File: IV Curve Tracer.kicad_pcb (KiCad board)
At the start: 2 copper layers, 130 x 80 mm, 75 parts, among them IC1 MAX680ESA+, J0 TB002-500-02BE, J1 CAN_Out, J5 Conn_01x15, J6 Conn_01x15, J7 CAN_In, Q1 IRF100P218XKMA1, Q2 IRF100P218XKMA1, SW0 SW_Rotary2x3, U1 INA211CQDCKRQ1, U2 LT1215, U3 LT1215, U4 ADM3055E, U5 CDSOT23-T24CAN

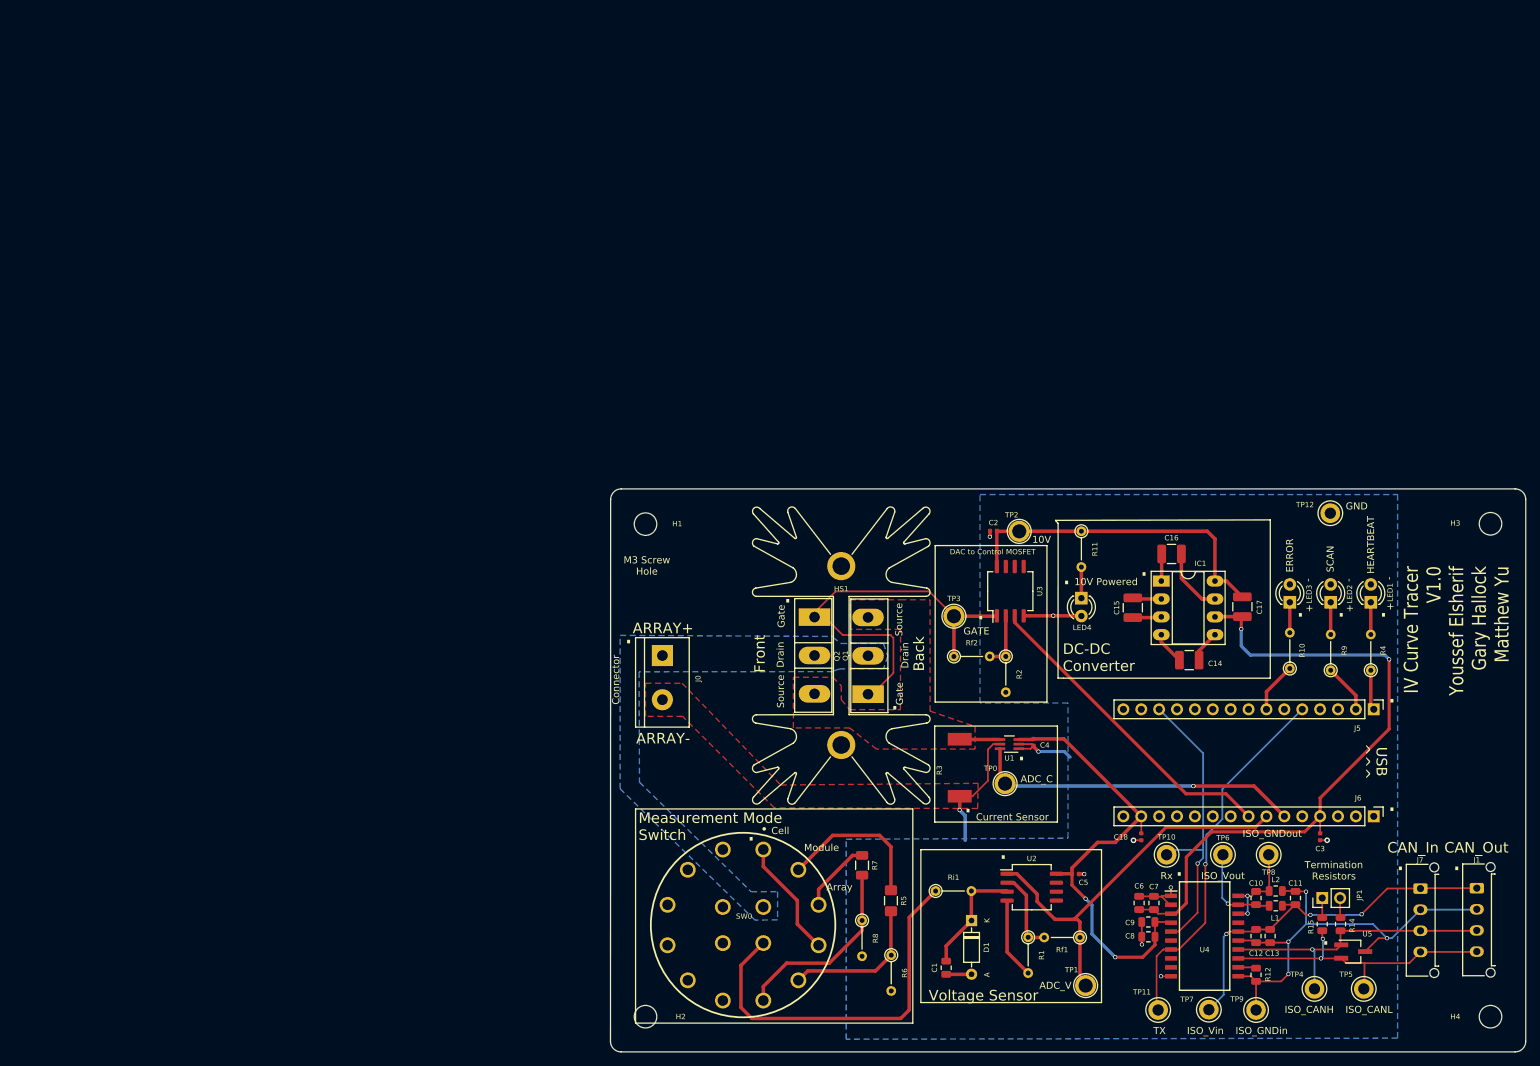
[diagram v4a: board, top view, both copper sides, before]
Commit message: Major Curve Tracer Board overhaul. Schematic advanced to Rev 1.1.0. Layout advanced to Rev 1.1.0. Parts list advanced to Rev 1.1.0.
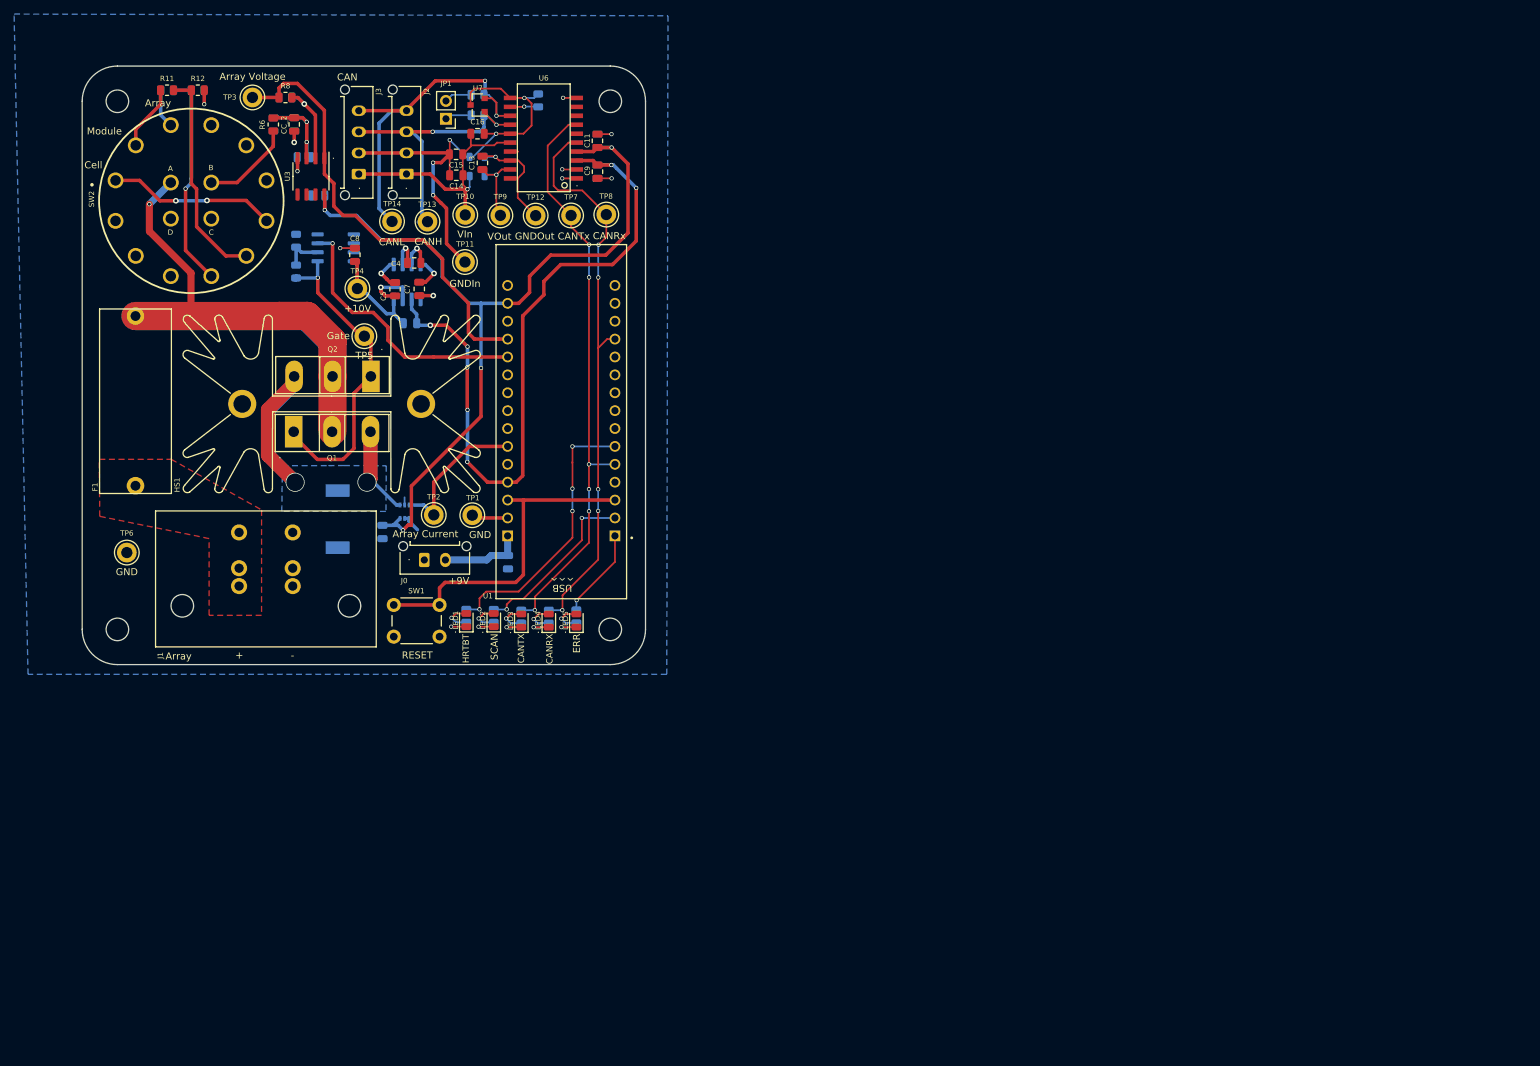
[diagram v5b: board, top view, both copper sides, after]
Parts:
- removed C17: 4.7uF, Capacitor_SMD:C_1210_3225Metric
- removed C18, C2: .1uF, Capacitor_SMD:C_0402_1005Metric
- removed IC1: MAX680ESA+, Package_DIP:DIP-8_W7.62mm_Socket_LongPads
- removed J5, J6: Conn_01x15, Connector_PinHeader_2.54mm:PinHeader_1x15_P2.54mm_Vertical
- removed J7: CAN_In, Connector_Molex:Molex_Micro-Fit_3.0_43650-0415_1x04_P3.00mm_Vertical
- removed Rf1: 1k, Resistor_THT:R_Axial_DIN0204_L3.6mm_D1.6mm_P5.08mm_Vertical
- removed Rf2: 4k, Resistor_THT:R_Axial_DIN0204_L3.6mm_D1.6mm_P5.08mm_Vertical
- removed Ri1: 10k, Resistor_THT:R_Axial_DIN0204_L3.6mm_D1.6mm_P5.08mm_Vertical
- removed SW0: SW_Rotary2x3, CK1052:CK1052
- removed TP0: TestPoint, TestPoint:TestPoint_Plated_Hole_D2.0mm
- added C0: .1uF, Capacitor_SMD:C_0805_2012Metric, B.Cu at (80.5, 90.5)
- added CA_2: .01uF, Capacitor_SMD:C_0805_2012Metric, B.Cu at (51.5, 32.9)
- added CB_2: .01uF, Capacitor_SMD:C_0805_2012Metric, B.Cu at (50.1, 28.3)
- added CC_2: .01uF, Capacitor_SMD:C_0805_2012Metric, F.Cu at (50.1, 28.3)
- added F1: Fuse, IV Curve Tracer:05200101Z_Fuze_Holder_5x20_PCB_Mount, F.Cu at (32.7, 54.5)
- added G***: LOGO, UTSVT_Special:UTSVT_Logo_Symbol, B.Cu at (88.2, 47.2)
- added G***: LOGO, UTSVT_Special:Hallock_Image_Small, B.Cu at (88.2, 75.6)
- added J2: CAN_In, Connector_Molex:Molex_Micro-Fit_3.0_43650-0415_1x04_P3.00mm_Vertical, F.Cu at (66.1, 35.3)
- added J3: CAN_Out, Connector_Molex:Molex_Micro-Fit_3.0_43650-0415_1x04_P3.00mm_Vertical, F.Cu at (59.3, 35.3)
- added LED5: Error (Amber), LED_SMD:LED_0805_2012Metric, F.Cu at (90.2, 98.8)
- added R13: 132k, Resistor_SMD:R_0805_2012Metric, B.Cu at (32.1, 23.4)
- added R16: 0, Resistor_SMD:R_0805_2012Metric, B.Cu at (84.8, 24.9)
- added R17: 60, Resistor_SMD:R_0805_2012Metric, B.Cu at (76.2, 27.0)
- added R18: 60, Resistor_SMD:R_0805_2012Metric, B.Cu at (76.2, 24.1)
- added SW1: SW_Push, Button_Switch_THT:SW_PUSH_6mm, F.Cu at (70.8, 101.0)
- added SW2: A20303RNCG, IV Curve Tracer:A20303RNCG_rotary_sw_dp3t, F.Cu at (35.5, 39.1)
- added TP13: CAN_H, TestPoint:TestPoint_Keystone_5005-5009_Compact, F.Cu at (69.0, 42.1)
- added TP14: CAN_L, TestPoint:TestPoint_Keystone_5005-5009_Compact, F.Cu at (64.0, 42.1)
- added U6: ADM3055E, IV Curve Tracer:ADM3055EBRIZ, F.Cu at (85.5, 30.2)
- added U7: CDSOT23-T24CAN, Package_TO_SOT_SMD:SOT-23, F.Cu at (76.2, 25.5)
- C1: value Variable -> .1uF; moved to B.Cu
- C10: value 0.22uF -> .1uF; moved to B.Cu
- C11: value 10uF -> .1uF
- C12: value 0.1uF -> .01uF; moved to B.Cu
- C13: value 0.01uF -> .22uF
- C14: value 4.7uF -> 10uF; footprint Capacitor_SMD:C_1210_3225Metric -> Capacitor_SMD:C_0805_2012Metric
- C15: value 4.7uF -> .1uF; footprint Capacitor_SMD:C_1210_3225Metric -> Capacitor_SMD:C_0805_2012Metric
- C16: value 4.7uF -> .01uF; footprint Capacitor_SMD:C_1210_3225Metric -> Capacitor_SMD:C_0805_2012Metric
- C3: footprint Capacitor_SMD:C_0402_1005Metric -> Capacitor_SMD:C_0805_2012Metric; moved to B.Cu
- C4, C5: value .1uF -> 4.7uF; footprint Capacitor_SMD:C_0402_1005Metric -> Capacitor_SMD:C_0805_2012Metric
- C6: value 10uF -> 4.7uF; moved to B.Cu
- C7: value 0.1uF -> 4.7uF
- C8: value 0.1uF -> .1uF
- C9: value 0.01uF -> 10uF
- D1: value 1N5226B-B -> 3.9V Zener; footprint Diode_THT:D_DO-35_SOD27_P7.62mm_Horizontal -> Diode_SMD:D_0805_2012Metric; moved to B.Cu
- J0: value TB002-500-02BE -> 9V Supply; footprint IV Curve Tracer:ExpandedBlockTerminal-2H_P7.62mm -> Connector_Molex:Molex_Micro-Fit_3.0_43650-0215_1x02_P3.00mm_Vertical
- J1: value CAN_Out -> Solar Array; footprint Connector_Molex:Molex_Micro-Fit_3.0_43650-0415_1x04_P3.00mm_Vertical -> IV Curve Tracer:PhoenixContact_PowerCombicon5_GF_2x7.62mm
- L1, L2: value 2kH -> 1.8kH; moved to B.Cu
- LED1: value TLHR5400-AS12Z -> Heartbeat (Blue); footprint LED_THT:LED_D3.0mm -> LED_SMD:LED_0805_2012Metric
- LED2: value TLHR5400-AS12Z -> Scanning (Blue); footprint LED_THT:LED_D3.0mm -> LED_SMD:LED_0805_2012Metric
- LED3: value TLHR5400-AS12Z -> CAN_Rx (Blue); footprint LED_THT:LED_D3.0mm -> LED_SMD:LED_0805_2012Metric
- LED4: value TLHR5400-AS12Z -> CAN_Tx (Blue); footprint LED_THT:LED_D3.0mm -> LED_SMD:LED_0805_2012Metric
- R1, R2: value 1k -> 330; footprint Resistor_THT:R_Axial_DIN0204_L3.6mm_D1.6mm_P5.08mm_Vertical -> Resistor_SMD:R_0805_2012Metric; moved to B.Cu
- R10: value 330 -> 1k; footprint Resistor_THT:R_Axial_DIN0204_L3.6mm_D1.6mm_P5.08mm_Vertical -> Resistor_SMD:R_0805_2012Metric; moved to B.Cu
- R11: value 1k -> 56.6k; footprint Resistor_THT:R_Axial_DIN0204_L3.6mm_D1.6mm_P5.08mm_Vertical -> Resistor_SMD:R_0805_2012Metric
- R12: value 0 -> 10k
- R14: value 60 -> 2k; moved to B.Cu
- R15: value 60 -> .5m; footprint Resistor_SMD:R_0805_2012Metric -> IV Curve Tracer:R-WSLF2512L5000FEB; moved to B.Cu
- R3: value R3: WSLF2512L5000FEB (.5mO) -> 330; footprint IV Curve Tracer:R-WSLF2512L5000FEB -> Resistor_SMD:R_0805_2012Metric; moved to B.Cu
- R4: footprint Resistor_THT:R_Axial_DIN0204_L3.6mm_D1.6mm_P5.08mm_Vertical -> Resistor_SMD:R_0805_2012Metric; moved to B.Cu
- R5: value R5: RN732BTTD56R6F50 (56.6k) -> 330; footprint Resistor_SMD:R_1206_3216Metric_Pad1.42x1.75mm_HandSolder -> Resistor_SMD:R_0805_2012Metric; moved to B.Cu
- R6: footprint Resistor_THT:R_Axial_DIN0204_L3.6mm_D1.6mm_P5.08mm_Vertical -> Resistor_SMD:R_0805_2012Metric
- R7: value R7: RN73H2BTTD1323F25 (132kO) -> 1k; footprint Resistor_SMD:R_1206_3216Metric -> Resistor_SMD:R_0805_2012Metric; moved to B.Cu
- R8: value 2k -> 1k; footprint Resistor_THT:R_Axial_DIN0204_L3.6mm_D1.6mm_P5.08mm_Vertical -> Resistor_SMD:R_0805_2012Metric
- R9: value 330 -> 4k; footprint Resistor_THT:R_Axial_DIN0204_L3.6mm_D1.6mm_P5.08mm_Vertical -> Resistor_SMD:R_0805_2012Metric; moved to B.Cu
- TP1: value TestPoint -> GND; footprint TestPoint:TestPoint_Plated_Hole_D2.0mm -> TestPoint:TestPoint_Keystone_5005-5009_Compact
- TP10: value CAN_Rx -> CAN_ISO_Vin
- TP11: value CAN_Tx -> CAN_ISO_GndIn
- TP12: value GroundTP -> CAN_ISO_GndOut
- TP2: value TestPoint -> Array Current; footprint TestPoint:TestPoint_Plated_Hole_D2.0mm -> TestPoint:TestPoint_Keystone_5005-5009_Compact
- TP3: value TestPoint -> Array Voltage; footprint TestPoint:TestPoint_Plated_Hole_D2.0mm -> TestPoint:TestPoint_Keystone_5005-5009_Compact
- TP4: value CAN_H -> +10V
- TP5: value CAN_L -> Gate
- TP6: value ISO_Vout -> GND
- TP7: value ISO_Vin -> CAN_Tx
- TP8: value ISO_GNDout -> CAN_Rx
- TP9: value ISO_GNDin -> CAN_ISO_Vout
- U1: value INA211CQDCKRQ1 -> MCU_Nucleo_L432KC; footprint Package_TO_SOT_SMD:SOT-363_SC-70-6_Handsoldering -> IV Curve Tracer:MODULE_NUCLEO-L432KC
- U2: value LT1215 -> INA211; footprint Package_SO:SO-8_5.3x6.2mm_P1.27mm -> IV Curve Tracer:SC70-6; moved to B.Cu
- U3: footprint Package_SO:SO-8_5.3x6.2mm_P1.27mm -> Package_SO:SO-8_3.9x4.9mm_P1.27mm
- U4: value ADM3055E -> MAX680ESA+; footprint SamacSys_Parts:SOIC127P1030X264-20N -> Package_SO:SOIC-8_3.9x4.9mm_P1.27mm; moved to B.Cu
- U5: value CDSOT23-T24CAN -> LT1215; footprint Package_TO_SOT_SMD:SOT-23W_Handsoldering -> Package_SO:SO-8_3.9x4.9mm_P1.27mm; moved to B.Cu
- moved R14 200.9 mm to (36.4, 23.4), turned to 0 degrees
- moved R12 195.9 mm to (36.4, 23.4), turned to 0 degrees
- moved H3 195.6 mm to (25.0, 100.0)
- moved J1 182.9 mm to (42.3, 86.2), turned to 0 degrees
- moved U5 175.7 mm to (56.0, 45.8)
- moved TP5 169.5 mm to (60.1, 58.4), turned to 180 degrees
- moved C3 168.9 mm to (53.5, 38.4), turned to 0 degrees
- moved TP4 168.4 mm to (59.1, 51.6), turned to 180 degrees
- moved JP1 166.5 mm to (71.7, 27.5), turned to 180 degrees
- moved TP6 161.5 mm to (26.3, 89.1)
- moved R9 157.5 mm to (50.4, 49.2)
- moved C13 156.7 mm to (76.8, 33.8), turned to 90 degrees
- moved TP9 155.7 mm to (79.4, 41.2)
- moved L2 154.1 mm to (76.1, 32.9), turned to 0 degrees
- moved R10 153.6 mm to (50.4, 44.8)
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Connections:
- C1 pad 1: GND -> +3V3
- C1 pad 2: Net-(C1-Pad2) -> GND
- C10 pad 1: Net-(C10-Pad1) -> +5V
- C10 pad 2: Net-(C10-Pad2) -> GND
- C11 pad 1: Net-(C11-Pad1) -> +3V3
- C11 pad 2: Net-(C11-Pad2) -> GND
- C12 pad 1: Net-(C11-Pad1) -> +3V3
- C12 pad 2: Net-(C11-Pad2) -> GND
- C13 pad 1: Net-(C11-Pad1) -> Net-(C13-Pad1)
- C13 pad 2: Net-(C11-Pad2) -> Net-(C13-Pad2)
- C14 pad 1: -10V -> Net-(C14-Pad1)
- C14 pad 2: GND -> Net-(C14-Pad2)
- C15 pad 1: Net-(C15-Pad1) -> Net-(C14-Pad1)
- C15 pad 2: Net-(C15-Pad2) -> Net-(C14-Pad2)
- C16 pad 1: Net-(C16-Pad1) -> Net-(C14-Pad1)
- C16 pad 2: Net-(C16-Pad2) -> Net-(C14-Pad2)
- C3 pad 1: +5V -> GND
- C3 pad 2: GND -> +3V3
- C4 pad 1: GND -> Net-(C4-Pad1)
- C4 pad 2: +3V3 -> Net-(C4-Pad2)
- C5 pad 1: GND -> Net-(C5-Pad1)
- C5 pad 2: +3V3 -> Net-(C5-Pad2)
- C6 pad 1: +5V -> +10V
- C6 pad 2: GND -> +5V
- C7 pad 1: +5V -> GND
- C7 pad 2: GND -> -10V
- C8 pad 1: +3V3 -> GND
- C8 pad 2: GND -> +10V
- C9 pad 1: +3V3 -> +5V
- D1 pad 1: Net-(C1-Pad2) -> Net-(CA_2-Pad1)
- J0 pad 1: Net-(J0-Pad1) -> GND
- J0 pad 2: GND -> +9V
- J1 pad 1: Net-(C11-Pad1) -> Net-(F1-Pad2)
- J1 pad 2: Net-(C11-Pad2) -> GND
- JP1 pad 1: /TERM_L -> Net-(JP1-Pad1)
- JP1 pad 2: /TERM_H -> Net-(JP1-Pad2)
- L1 pad 1: Net-(C11-Pad1) -> Net-(C14-Pad1)
- L1 pad 2: Net-(C10-Pad1) -> Net-(C13-Pad1)
- L2 pad 1: Net-(C11-Pad2) -> Net-(C14-Pad2)
- L2 pad 2: Net-(C10-Pad2) -> Net-(C13-Pad2)
- LED1 pad 1: Net-(LED1-Pad1) -> GND
- LED1 pad 2: GND -> Net-(LED1-Pad2)
- LED2 pad 1: Net-(LED2-Pad1) -> GND
- LED2 pad 2: GND -> Net-(LED2-Pad2)
- LED3 pad 1: Net-(LED3-Pad1) -> GND
- LED3 pad 2: GND -> Net-(LED3-Pad2)
- LED4 pad 1: Net-(LED4-Pad1) -> GND
- LED4 pad 2: GND -> Net-(LED4-Pad2)
- Q1 pad 1: GATE -> /Gate
- Q1 pad 2: Net-(J0-Pad1) -> Net-(F1-Pad1)
- Q1 pad 3: Net-(Q1-Pad3) -> /+Current_Sense
- Q2 pad 1: GATE -> /Gate
- Q2 pad 2: Net-(J0-Pad1) -> Net-(F1-Pad1)
- Q2 pad 3: Net-(Q1-Pad3) -> /+Current_Sense
- R1 pad 1: Net-(R1-Pad1) -> Net-(LED1-Pad2)
- R1 pad 2: GND -> /Heartbeat
- R10 pad 1: Net-(J5-Pad7) -> Net-(R10-Pad1)
- R10 pad 2: Net-(LED3-Pad1) -> GND
- R11 pad 1: +10V -> Net-(R11-Pad1)
- R11 pad 2: Net-(LED4-Pad1) -> Net-(R11-Pad2)
- R12 pad 1: /RSlope -> Net-(R11-Pad2)
- R12 pad 2: Net-(C11-Pad2) -> GND
- R14 pad 1: /TERM_H -> Net-(R13-Pad2)
- R14 pad 2: /CAN_H -> GND
- R15 pad 1: /TERM_L -> GND
- R15 pad 2: /CAN_L -> /+Current_Sense
- R2 pad 1: Net-(R2-Pad1) -> Net-(LED2-Pad2)
- R2 pad 2: GND -> /Scanning
- R3 pad 1: GND -> Net-(LED3-Pad2)
- R3 pad 2: Net-(Q1-Pad3) -> /CAN_Rx
- R4 pad 1: Net-(J5-Pad1) -> Net-(LED4-Pad2)
- R4 pad 2: Net-(LED1-Pad1) -> /CAN_Tx
- R5 pad 2: Net-(R5-Pad2) -> /Error
- R6 pad 1: Net-(R5-Pad2) -> /Voltage_Sense
- R6 pad 2: GND -> Net-(CA_2-Pad1)
- R7 pad 2: Net-(R7-Pad2) -> GND
- R8 pad 1: Net-(R7-Pad2) -> /Array_Voltage
- R8 pad 2: GND -> Net-(R7-Pad1)
- R9 pad 1: Net-(J5-Pad2) -> /Gate
- R9 pad 2: Net-(LED2-Pad1) -> Net-(R10-Pad1)
- TP1 pad 1: ADC_V -> GND
- TP10 pad 1: CAN_RX -> Net-(C14-Pad1)
- TP11 pad 1: CAN_TX -> Net-(C14-Pad2)
- TP12 pad 1: GND -> Net-(C13-Pad2)
- TP2 pad 1: +10V -> /Array_Current
- TP3 pad 1: GATE -> /Array_Voltage
- TP4 pad 1: /CAN_H -> +10V
- TP5 pad 1: /CAN_L -> /Gate
- TP6 pad 1: Net-(C10-Pad1) -> GND
- TP7 pad 1: Net-(C11-Pad1) -> /CAN_Tx
- TP8 pad 1: Net-(C10-Pad2) -> /CAN_Rx
- TP9 pad 1: Net-(C11-Pad2) -> Net-(C13-Pad1)
- U1 pad 1: GND -> /Error
- U1 pad 2: GND -> /Scanning
- U1 pad 3: +3V3 -> /Reset
- U1 pad 4: Net-(Q1-Pad3) -> GND
- U1 pad 5: GND -> /CAN_Tx
- U1 pad 6: ADC_C -> /Heartbeat
- U2 pad 1: ADC_V -> GND
- U2 pad 2: Net-(R1-Pad1) -> GND
- U2 pad 3: Net-(C1-Pad2) -> +3V3
- U2 pad 4: GND -> /+Current_Sense
- U2 pad 5: Net-(U2-Pad5) -> GND
- U2 pad 6: Net-(U2-Pad6) -> /Array_Current
- U3 pad 1: GATE -> /Array_Voltage
- U3 pad 2: Net-(R2-Pad1) -> Net-(R7-Pad1)
- U3 pad 3: DAC_Control -> Net-(CA_2-Pad1)
- U3 pad 8: +10V -> +3V3
- U4 pad 1: GND -> Net-(C5-Pad1)
- U4 pad 2: GND -> Net-(C4-Pad2)
- U4 pad 3: +5V -> Net-(C4-Pad1)
- U4 pad 4: +3V3 -> -10V
- U4 pad 5: CAN_RX -> GND
- U4 pad 6: Net-(U4-Pad6) -> +5V
- U4 pad 7: CAN_TX -> Net-(C5-Pad2)
- U4 pad 8: Net-(U4-Pad8) -> +10V
- U5 pad 1: /CAN_H -> /Gate
- U5 pad 2: /CAN_L -> Net-(R10-Pad1)
- U5 pad 3: Net-(C11-Pad2) -> /DAC_Control
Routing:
- net Net-(F1-Pad1): track 0.00 -> 99.5 mm, vias 0 -> 1
- net /CAN_Tx: track 0.00 -> 82.6 mm, vias 0 -> 6
- net /CAN_Rx: track 0.00 -> 81.0 mm, vias 0 -> 5
- net Net-(C14-Pad2): track 0.00 -> 69.9 mm, vias 0 -> 5
- net Net-(C11-Pad2): track 66.3 -> 0.00 mm, vias 4 -> 0
- net /Array_Voltage: track 0.00 -> 64.2 mm
- net GATE: track 58.6 -> 0.00 mm
- net ADC_V: track 56.6 -> 0.00 mm
- net /+Current_Sense: track 0.00 -> 56.1 mm, vias 0 -> 2
- net +3V3: track 66.7 -> 121.8 mm, vias 2 -> 4
- net Net-(Ri1-Pad1): track 53.9 -> 0.00 mm
- net Net-(C11-Pad1): track 53.2 -> 0.00 mm, vias 3 -> 0
- net CAN_TX: track 52.6 -> 0.00 mm, vias 1 -> 0
- net Net-(J2-Pad4): track 0.00 -> 51.0 mm, vias 0 -> 2
- net /Reset: track 0.00 -> 47.4 mm
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- added copper zone on B.Cu, net /+Current_Sense
- added copper zone on F.Cu, net Net-(F1-Pad2)
- removed copper zone on F.Cu, net GND
- removed copper zone on B.Cu, net Net-(J0-Pad1)
- removed copper zone on F.Cu, net Net-(Q1-Pad3)
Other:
- board size 130 x 80 mm -> 80 x 85 mm
- board text added: "+10V"
- board text added: "+9V"
- board text added: "Array Current"
- board text added: "Array Voltage"
- board text added: "CAN"
- board text added: "CANH"
- board text added: "CANL"
- board text added: "CANRX"
- board text added: "CANRx"
- board text added: "CANTX"
- board text added: "CANTx"
- board text added: "ERR"
- board text added: "GNDIn"
- board text added: "GNDOut"
- board text added: "HRTBT"
- board text added: "RESET"
- board text added: "Separating high power fluctuations from digital and analog signals."
- board text added: "This looks a little odd, but hopefully it protects the analog signal a little bit from power and digital fluctuations."
- board text added: "UTSVT - Array PV Curve Tracer Board v1.0 Fall 2020 Youssef Elsherif Gary Hallock Matthew Yu"
- board text added: "VIn"
- board text added: "VOut"
- board text added: "We get pretty tight here."
- board text added: "Wide trace to reduce resistance and voltage drop as much as possible"
- board text removed: "10V"
- board text removed: "10V Powered"
- board text removed: "A"
- board text removed: "ADC_C"
- board text removed: "ADC_V"
- board text removed: "ARRAY+"
- board text removed: "ARRAY-"
- board text removed: "Back"
- board text removed: "CAN_In"
- board text removed: "CAN_Out"
- board text removed: "Connector"
- board text removed: "Current Sensor"
- board text removed: "DAC to Control MOSFET"
- board text removed: "DC-DC Converter"
- board text removed: "Drain"
- board text removed: "ERROR"
- board text removed: "Front"
- board text removed: "GATE"
- board text removed: "HEARTBEAT"
- board text removed: "ISO_CANH"
- board text removed: "ISO_CANL"
- board text removed: "ISO_GNDin"
- board text removed: "ISO_GNDout"
- board text removed: "ISO_Vin"
- board text removed: "ISO_Vout"
- board text removed: "IV Curve Tracer V1.0 Youssef Elsherif Gary Hallock Matthew Yu"
- board text removed: "M3 Screw Hole"
- board text removed: "Measurement Mode Switch"
- board text removed: "Rx"
- board text removed: "Source"
- board text removed: "TX"
- board text removed: "Termination Resistors"
- board text removed: "Voltage Sensor"

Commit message: Addressed review.
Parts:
- removed the C1 at (62.6, 86.2)
- removed the C8 at (58.7, 46.8)
- removed the U5 at (56.0, 45.8)
- added C2: 0.1uF, Capacitor_SMD:C_0805_2012Metric, B.Cu at (65.2, 85.2)
- added C3: 1uF, Capacitor_SMD:C_0805_2012Metric, B.Cu at (68.6, 73.1)
- added D1: 3.9V Zener, Diode_SMD:D_SOD-123F, B.Cu at (75.2, 72.6)
- added D2: Diode, Diode_SMD:D_SOD-123F, B.Cu at (71.8, 72.6)
- added D4: Diode, Diode_SMD:D_SOD-123F, F.Cu at (67.6, 42.4)
- added R7: 1.7k, Resistor_SMD:R_0805_2012Metric, B.Cu at (68.6, 77.5)
- added TP1: 9V, TestPoint:TestPoint_Keystone_5005-5009_Compact, F.Cu at (75.8, 90.2)
- C1: renamed from C0; value .1uF -> 0.1uF
- C11: renamed from C7; moved to B.Cu
- C4: renamed from CA_2; value .01uF -> 1uF
- C5: renamed from CB_2; value .01uF -> 0.1uF
- C6: renamed from CC_2; value .01uF -> 0.01uF
- C7: renamed from C3; value .1uF -> 0.1uF
- C8: renamed from C4; moved to B.Cu
- C9: renamed from C5; moved to B.Cu
- D3: renamed from D1; footprint Diode_SMD:D_0805_2012Metric -> Diode_SMD:D_SOD-123F
- R6: renamed from R15; value .5m -> 2m; footprint IV Curve Tracer:R-WSLF2512L5000FEB -> Resistor_SMD:R_1206_3216Metric
- TP3: renamed from TP2; value Array Current -> Array_I
- U2: value INA211 -> INA210
- U4: moved to F.Cu
- moved TP4 38.5 mm to (75.5, 46.9)
- moved TP14 27.3 mm to (48.2, 24.4)
- moved TP12 27.3 mm to (53.3, 30.5)
- moved D3 24.9 mm to (67.6, 42.5)
- moved R10 22.3 mm to (63.7, 41.1), turned to 180 degrees
- moved R9 22.3 mm to (63.7, 41.1), turned to 0 degrees
- moved TP15 20.6 mm to (53.2, 24.5)
- moved C5 9.92 mm to (52.5, 37.9), turned to 180 degrees
- moved C6 9.91 mm to (52.5, 37.9), turned to 180 degrees
- moved U3 9.33 mm to (51.8, 45.0)
- moved R8 8.57 mm to (52.5, 35.0), turned to 0 degrees
- moved C10 5.99 mm to (62.0, 52.6), turned to 90 degrees
- moved C11 5.84 mm to (62.7, 48.9), turned to 0 degrees
- moved C7 5.80 mm to (54.5, 44.1), turned to 270 degrees
- moved R4 3.91 mm to (82.4, 98.1)
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- renumbered C6 to C10, C9 to C12, C10 to C13, C11 to C14, C12 to C15, C13 to C16, C14 to C17, C15 to C18, C16 to C19, J0 to J1, J1 to J2, J2 to J3, J3 to J4, R8 to R10, R9 to R11, R10 to R12, R11 to R13, R12 to R14, R13 to R15, R14 to R16, R16 to R17, R17 to R18, R18 to R19, R6 to R8, R7 to R9, TP9 to TP10, TP10 to TP11, TP11 to TP12, TP12 to TP13, TP13 to TP14, TP14 to TP15, TP1 to TP2, TP3 to TP4, TP4 to TP5, TP5 to TP6, TP6 to TP7, TP7 to TP8, TP8 to TP9, U6 to U5, U7 to U6
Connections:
- C4 pad 1: Net-(CA_2-Pad1) -> Net-(C4-Pad1)
- C5 pad 1: Net-(CA_2-Pad1) -> Net-(C4-Pad1)
- C6 pad 1: Net-(CA_2-Pad1) -> Net-(C4-Pad1)
- C7 pad 2: +3V3 -> +10V
- D3 pad 1: Net-(CA_2-Pad1) -> /Array_Voltage
- R11 pad 2: Net-(R10-Pad1) -> Net-(R11-Pad2)
- R12 pad 1: Net-(R10-Pad1) -> Net-(R11-Pad2)
- R8 pad 2: Net-(CA_2-Pad1) -> Net-(C4-Pad1)
- U1 pad 20: /DAC_Control -> Net-(U1-Pad20)
- U1 pad 22: Net-(U1-Pad22) -> /DAC_Control
- U2 pad 3: +3V3 -> +9V
- U2 pad 6: /Array_Current -> Net-(R7-Pad2)
- U3 pad 3: Net-(CA_2-Pad1) -> Net-(C4-Pad1)
- U3 pad 5: Net-(U3-Pad5) -> /DAC_Control
- U3 pad 6: Net-(U3-Pad6) -> Net-(R11-Pad2)
- U3 pad 7: Net-(U3-Pad7) -> /Gate
- U3 pad 8: +3V3 -> +10V
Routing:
- net +3V3: track 121.8 -> 42.9 mm, vias 4 -> 1
- net /Array_Voltage: track 64.2 -> 43.6 mm, vias 0 -> 1
- net Net-(CA_2-Pad1): track 17.6 -> 0.00 mm, vias 2 -> 0
- net Net-(C4-Pad1): track 0.00 -> 15.7 mm, vias 0 -> 2
- net Net-(C17-Pad2): track 69.9 -> 57.2 mm, vias 5 -> 3
- net Net-(J3-Pad4): track 51.0 -> 38.5 mm
- net /DAC_Control: track 38.9 -> 50.7 mm
- net +5V: track 102.0 -> 113.0 mm, vias 7 -> 4
- net +9V: track 12.3 -> 23.0 mm
- net Net-(R11-Pad2): track 0.00 -> 7.49 mm, vias 0 -> 1
- net Net-(R10-Pad1): track 5.91 -> 0.00 mm
- net Net-(R7-Pad2): track 0.00 -> 5.72 mm
- net +10V: track 18.5 -> 23.5 mm
- net Net-(C17-Pad1): track 36.5 -> 41.2 mm, vias 1 -> 0
- net Net-(C9-Pad2): track 7.71 -> 4.45 mm
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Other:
- board text added: "ARR_V"
- board text added: "UTSVT - Array PV Curve Tracer Board v1.1 Fall 2020 Youssef Elsherif Gary Hallock Matthew Yu"
- board text removed: "Array Voltage"
- board text removed: "UTSVT - Array PV Curve Tracer Board v1.0 Fall 2020 Youssef Elsherif Gary Hallock Matthew Yu"

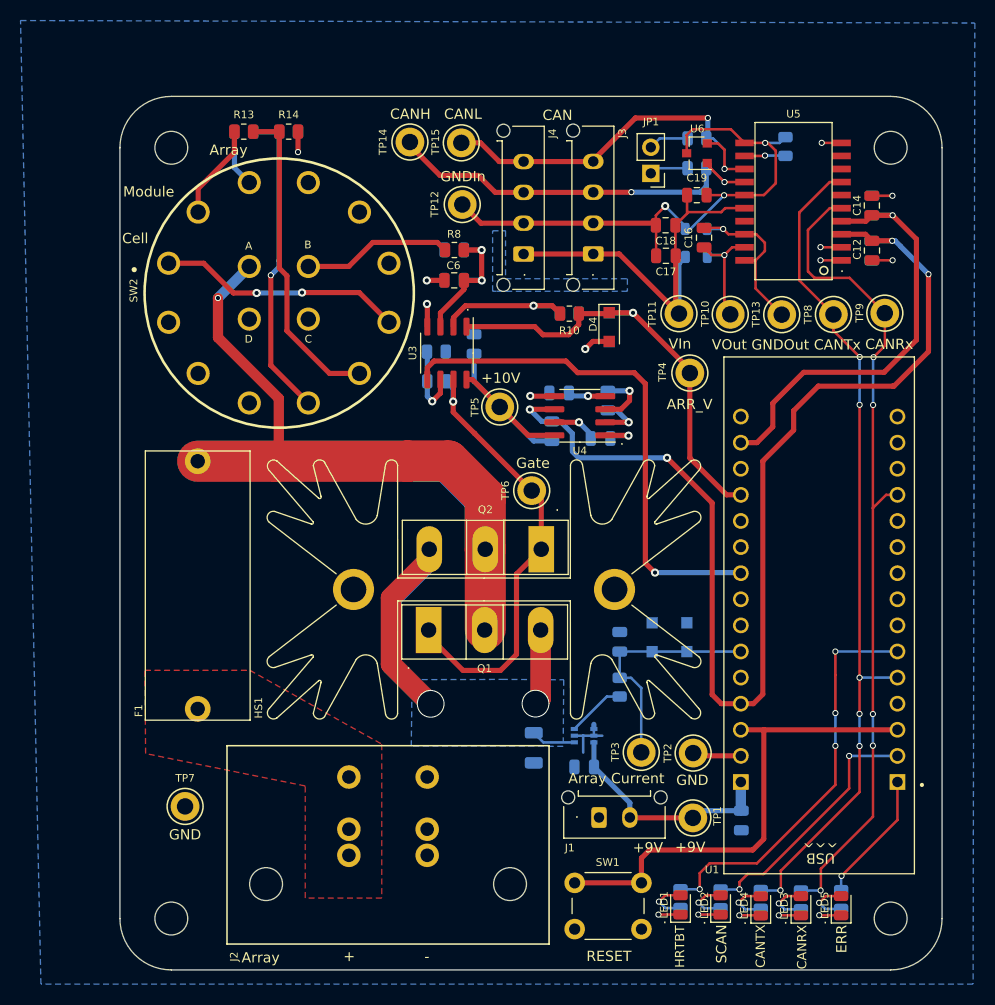
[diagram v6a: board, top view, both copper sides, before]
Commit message: added bodge notes to current version Curve Tracer
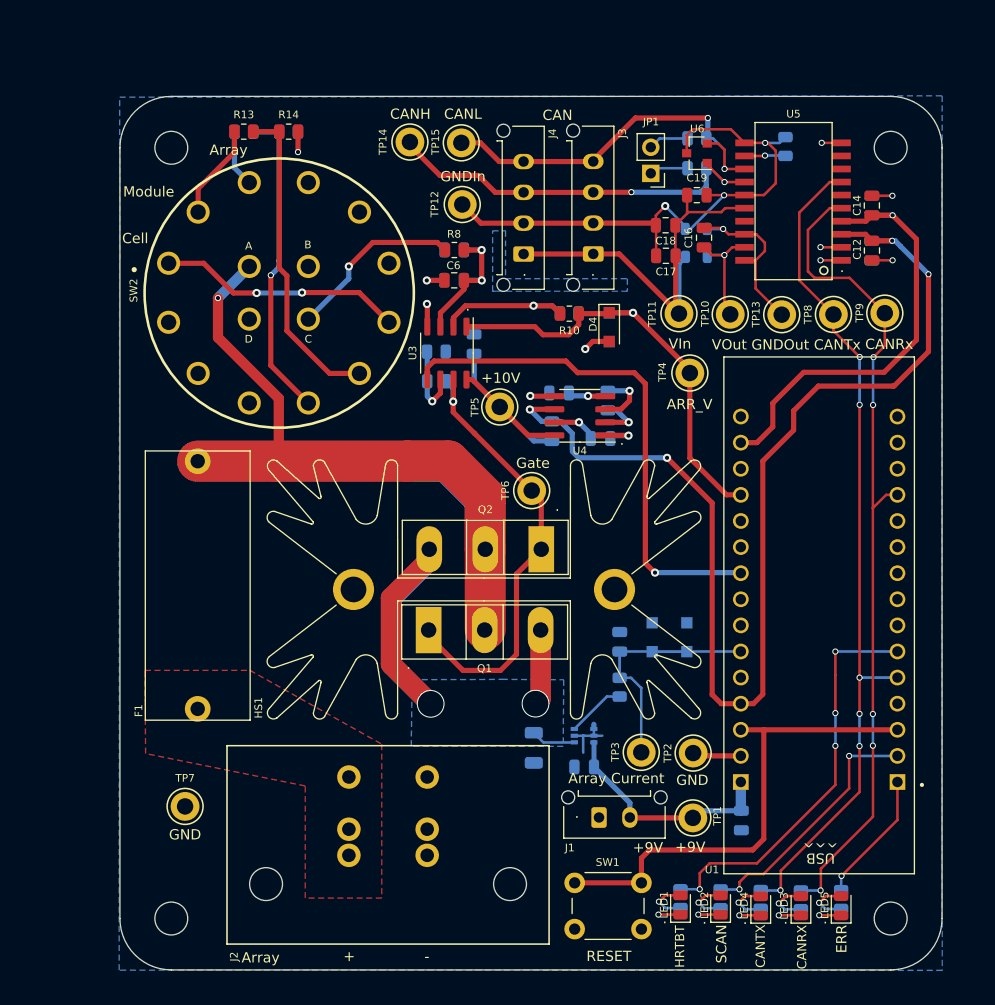
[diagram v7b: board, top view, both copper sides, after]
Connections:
- SW2 pad 14: /Voltage_Sense -> (no net)
- SW2 pad 15: (no net) -> /Voltage_Sense
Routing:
- net /Voltage_Sense: track 14.6 -> 17.4 mm, vias 0 -> 1
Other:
- rule pad_to_mask_clearance: 0.05 -> 0
- board text added: "U2"
